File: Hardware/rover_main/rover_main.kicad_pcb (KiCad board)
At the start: 2 copper layers, 80 x 70 mm, 19 parts, among them J1 BATT, J2 BME280, J3 CSS811, J4 DRIVERS, J7 FTDI, J8 PROG, U1 LD1117A33, U2 MCP732831CHARGER, U3 ESP32-CAM

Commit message: change diode in pcb
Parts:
- moved D1 10.5 mm to (142.5, 92.5), turned to 0 degrees
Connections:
- C1 pad 1: Net-(C1-Pad1) -> VCC
- D1 pad 1: Net-(C1-Pad1) -> VCC
- D1 pad 2: VCC -> /BATT
- U1 pad 3: Net-(C1-Pad1) -> VCC
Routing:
- net VCC: track 49.2 -> 70.6 mm
- net Net-(C1-Pad1): track 14.9 -> 0.00 mm
- net /BATT: track 12.1 -> 24.7 mm

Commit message: Asig. places componets
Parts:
- added J10: Analog, Connector_PinHeader_2.54mm:PinHeader_1x12_P2.54mm_Vertical, F.Cu at (167.0, 97.2)
- added J5: GY-87, Connector_PinHeader_2.54mm:PinHeader_1x08_P2.54mm_Vertical, F.Cu at (146.2, 113.8)
- added J6: PROG, Connector_PinSocket_2.54mm:PinSocket_1x02_P2.54mm_Vertical, F.Cu at (131.9, 117.7)
- added J9: i2c, Connector_PinHeader_2.54mm:PinHeader_1x02_P2.54mm_Vertical, F.Cu at (163.6, 80.7)
- added JP1: Engine 2B, Jumper:SolderJumper-2_P1.3mm_Bridged_RoundedPad1.0x1.5mm, B.Cu at (124.4, 83.0)
- added JP10: Engine 2B, Jumper:SolderJumper-2_P1.3mm_Open_RoundedPad1.0x1.5mm, B.Cu at (144.4, 88.1)
- added JP11: SDE ESP, Jumper:SolderJumper-2_P1.3mm_Bridged_RoundedPad1.0x1.5mm, B.Cu at (120.0, 100.8)
- added JP12: SCL ESP, Jumper:SolderJumper-2_P1.3mm_Bridged_RoundedPad1.0x1.5mm, B.Cu at (120.2, 98.1)
- added JP2: Engine 1A, Jumper:SolderJumper-2_P1.3mm_Bridged_RoundedPad1.0x1.5mm, B.Cu at (131.9, 83.0)
- added JP3: Engine 2A, Jumper:SolderJumper-2_P1.3mm_Bridged_RoundedPad1.0x1.5mm, B.Cu at (126.9, 83.0)
- added JP4: Engine 1B, Jumper:SolderJumper-2_P1.3mm_Bridged_RoundedPad1.0x1.5mm, B.Cu at (129.4, 83.0)
- added JP5: SDA, Jumper:SolderJumper-2_P1.3mm_Open_RoundedPad1.0x1.5mm, B.Cu at (157.2, 80.7)
- added JP6: SCL, Jumper:SolderJumper-2_P1.3mm_Open_RoundedPad1.0x1.5mm, B.Cu at (157.2, 78.2)
- added JP7: Engine 1A, Jumper:SolderJumper-2_P1.3mm_Open_RoundedPad1.0x1.5mm, B.Cu at (144.4, 93.2)
- added JP8: Engine 1B, Jumper:SolderJumper-2_P1.3mm_Open_RoundedPad1.0x1.5mm, B.Cu at (144.4, 95.6)
- added JP9: Engine 2A, Jumper:SolderJumper-2_P1.3mm_Open_RoundedPad1.0x1.5mm, B.Cu at (144.4, 90.6)
- J8: value PROG -> Digital; footprint Connector_PinSocket_2.54mm:PinSocket_1x02_P2.54mm_Vertical -> Connector_PinHeader_2.54mm:PinHeader_1x12_P2.54mm_Vertical
- moved D2 76.2 mm to (175.7, 129.8), turned to 90 degrees
- moved J2 67.9 mm to (163.5, 123.1), turned to 270 degrees
- moved R1 66.6 mm to (182.2, 122.8), turned to 270 degrees
- moved J3 55.3 mm to (131.5, 123.0), turned to 90 degrees
- moved C3 53.8 mm to (181.9, 75.2), turned to 180 degrees
- moved U1 53.6 mm to (183.6, 116.6), turned to 90 degrees
- moved J8 50.9 mm to (151.8, 69.2), turned to 0 degrees
- moved J4 45.2 mm to (121.9, 77.9), turned to 90 degrees
- moved C2 44.6 mm to (175.4, 116.6), turned to 270 degrees
- moved REF** 40.2 mm to (196.5, 140.0)
- moved U2 35.6 mm to (179.7, 88.1), turned to 0 degrees
- moved REF** 34.9 mm to (196.5, 70.0)
- moved J1 34.5 mm to (191.9, 82.4), turned to 270 degrees
- moved D1 34.3 mm to (174.7, 104.5)
- moved C1 34.0 mm to (175.3, 109.9), turned to 270 degrees
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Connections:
- J8 pad 1: /GPIO0 -> /RX
- J8 pad 2: GND -> /TX
- U3 pad 11: /GPIO12 -> /GPIO12E
- U3 pad 12: /GPIO13 -> /GPIO13E
- U3 pad 13: /GPIO15 -> /GPIO15E
- U3 pad 14: /GPIO14 -> /GPIO14E
- U3 pad 15: /SDA -> /SDAE
- U3 pad 7: /SCL -> /SCLE
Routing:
- net +3V3: track 126.8 -> 10.6 mm
- net /SCLE: track 0.00 -> 78.1 mm
- net VCC: track 70.6 -> 0.00 mm
- net /SCL: track 70.3 -> 0.00 mm
- net /SDA: track 42.9 -> 0.00 mm
- net /GPIO12: track 51.2 -> 12.8 mm
- net /GPIO13: track 52.9 -> 17.2 mm
- net /GPIO14: track 59.9 -> 25.1 mm
- net /GPIO15: track 55.8 -> 21.3 mm
- net /BATT: track 24.7 -> 0.00 mm
- net /RX: track 14.6 -> 0.00 mm
- net /TX: track 14.6 -> 0.00 mm
- net GND: track 12.0 -> 0.00 mm
- net /GPIO14E: track 0.00 -> 5.29 mm
- net /GPIO12E: track 0.00 -> 5.29 mm
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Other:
- board size 80 x 70 mm -> 100 x 80 mm

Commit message: RE-ROUTEO
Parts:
- removed the REF** at (106.0, 140.0)
- removed the REF** at (106.5, 70.0)
- removed the REF** at (196.5, 70.0)
- removed the REF** at (196.5, 140.0)
- added REF**: MountingHole_3.2mm_M3_Pad_Via, MountingHole:MountingHole_3.2mm_M3_Pad_Via, F.Cu at (105.0, 125.0)
- added REF**: MountingHole_3.2mm_M3_Pad_Via, MountingHole:MountingHole_3.2mm_M3_Pad_Via, F.Cu at (105.0, 65.1)
- added REF**: MountingHole_3.2mm_M3_Pad_Via, MountingHole:MountingHole_3.2mm_M3_Pad_Via, F.Cu at (180.5, 65.0)
- added REF**: MountingHole_3.2mm_M3_Pad_Via, MountingHole:MountingHole_3.2mm_M3_Pad_Via, F.Cu at (180.0, 125.0)
- J2: footprint Connector_PinHeader_2.54mm:PinHeader_1x04_P2.54mm_Vertical -> Connector_PinHeader_2.54mm:PinHeader_1x06_P2.54mm_Vertical
- moved JP6 27.1 mm to (152.1, 104.8), turned to 270 degrees
- moved J2 25.7 mm to (139.4, 114.3)
- moved JP8 24.4 mm to (135.9, 72.8), turned to 90 degrees
- moved JP5 24.2 mm to (154.7, 104.8), turned to 270 degrees
- moved JP12 21.7 mm to (141.0, 104.5), turned to 270 degrees
- moved JP7 21.3 mm to (138.4, 72.8), turned to 90 degrees
- moved JP11 18.8 mm to (138.4, 104.5), turned to 270 degrees
- moved JP9 18.2 mm to (141.0, 72.8), turned to 90 degrees
- moved J1 16.6 mm to (179.0, 72.0)
- moved J3 15.8 mm to (144.8, 114.2)
- moved JP10 15.4 mm to (143.5, 72.8), turned to 90 degrees
- moved C3 12.1 mm to (170.0, 77.1), turned to 90 degrees
- moved U3 10.8 mm to (124.7, 89.8)
- moved D2 10.5 mm to (168.4, 122.3), turned to 0 degrees
- moved JP1 10.5 mm to (122.6, 72.8)
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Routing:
- net +3V3: track 10.6 -> 168.8 mm, vias 0 -> 1
- net VCC: track 0.00 -> 157.8 mm, vias 0 -> 2
- net /RX: track 0.00 -> 87.4 mm
- net /TX: track 0.00 -> 86.0 mm
- net /SDAB: track 0.00 -> 76.2 mm, vias 0 -> 1
- net /SCLB: track 0.00 -> 73.4 mm, vias 0 -> 1
- net /SCLE: track 78.1 -> 13.1 mm
- net /A1: track 0.00 -> 58.9 mm
- net /A3: track 0.00 -> 58.7 mm
- net /11: track 0.00 -> 52.3 mm
- net /SDAE: track 0.00 -> 49.7 mm
- net /SDA: track 0.00 -> 48.6 mm
- net /SCL: track 0.00 -> 40.8 mm
- net /BATT: track 0.00 -> 26.7 mm
- net /9: track 0.00 -> 24.0 mm
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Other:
- board size 100 x 80 mm -> 85 x 70 mm

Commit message: Update traces
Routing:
- net +3V3: track 168.8 -> 182.7 mm
- net /SCL: track 40.8 -> 52.4 mm
- net /TX: track 86.0 -> 77.5 mm
- net /RX: track 87.4 -> 79.6 mm
- net /SDA: track 48.6 -> 51.7 mm
- net /A3: track 58.7 -> 61.6 mm
- net /11: track 52.3 -> 55.2 mm
- net /A1: track 58.9 -> 61.4 mm
- net /SDAB: track 76.2 -> 77.2 mm
- net /BATT: track 26.7 -> 26.2 mm
- net VCC: track 157.8 -> 157.9 mm, vias 2 -> 0
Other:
- net class Default: clearance 0.2 -> 0.3
- rule trace_clearance: 0.2 -> 0.3

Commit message: Labels
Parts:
- moved JP5 0.22 mm to (154.7, 104.5)
- moved JP6 0.22 mm to (152.1, 104.5)
- renumbered J9 to I2C
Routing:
- net /SCLE: track 13.1 -> 10.4 mm
- net /SDAB: track 77.2 -> 78.0 mm
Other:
- outline, holes or cut-outs redrawn
- board text added: "3V3"
- board text added: "A"
- board text added: "B"
- board text added: "BAST PRO-MINI"
- board text added: "CHARGER"
- board text added: "CTS"
- board text added: "DRIVERS BATS"
- board text added: "DRIVERS ESP"
- board text added: "DTR"
- board text added: "ENGINES"
- board text added: "Engine 1"
- board text added: "Engine 2"
- board text added: "GND"
- board text added: "I2C BATS"
- board text added: "I2C ESP"
- board text added: "RX"
- board text added: "TX"
- board text added: "VCC"

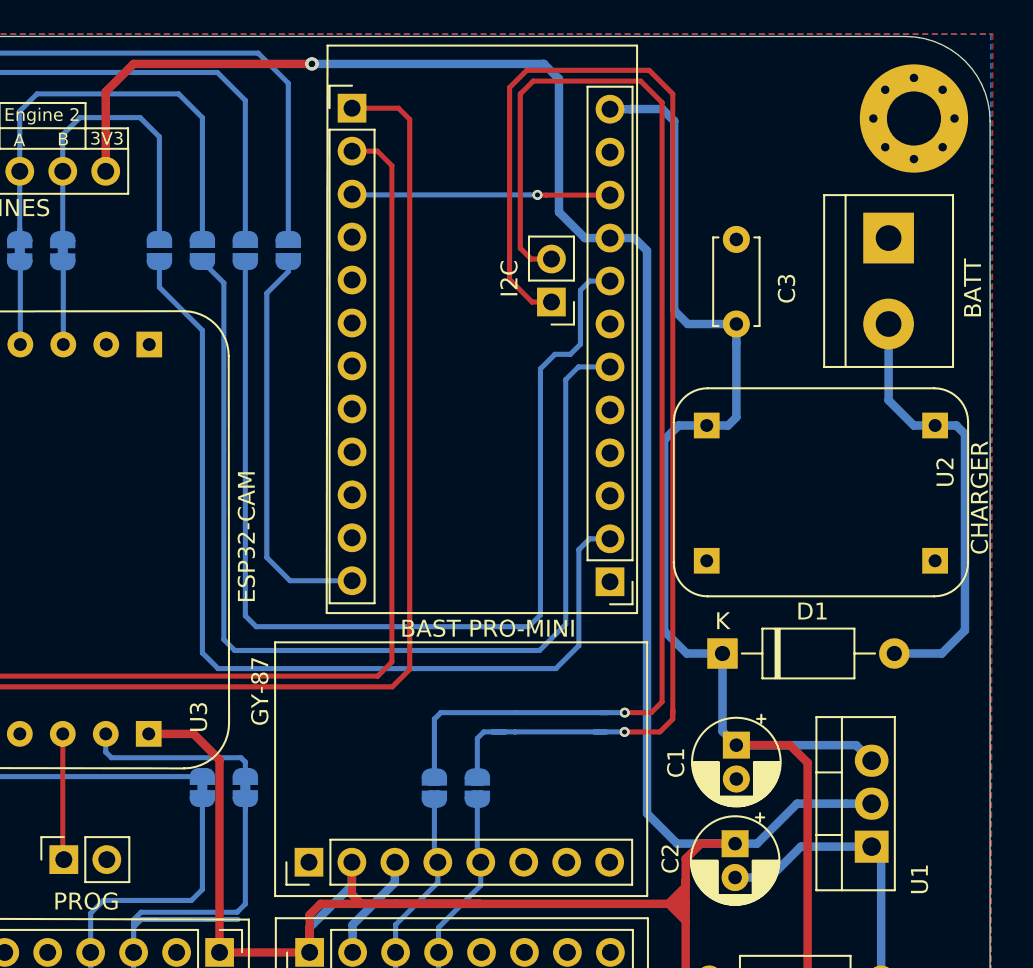
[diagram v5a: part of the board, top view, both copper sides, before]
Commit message: ADD DIODE
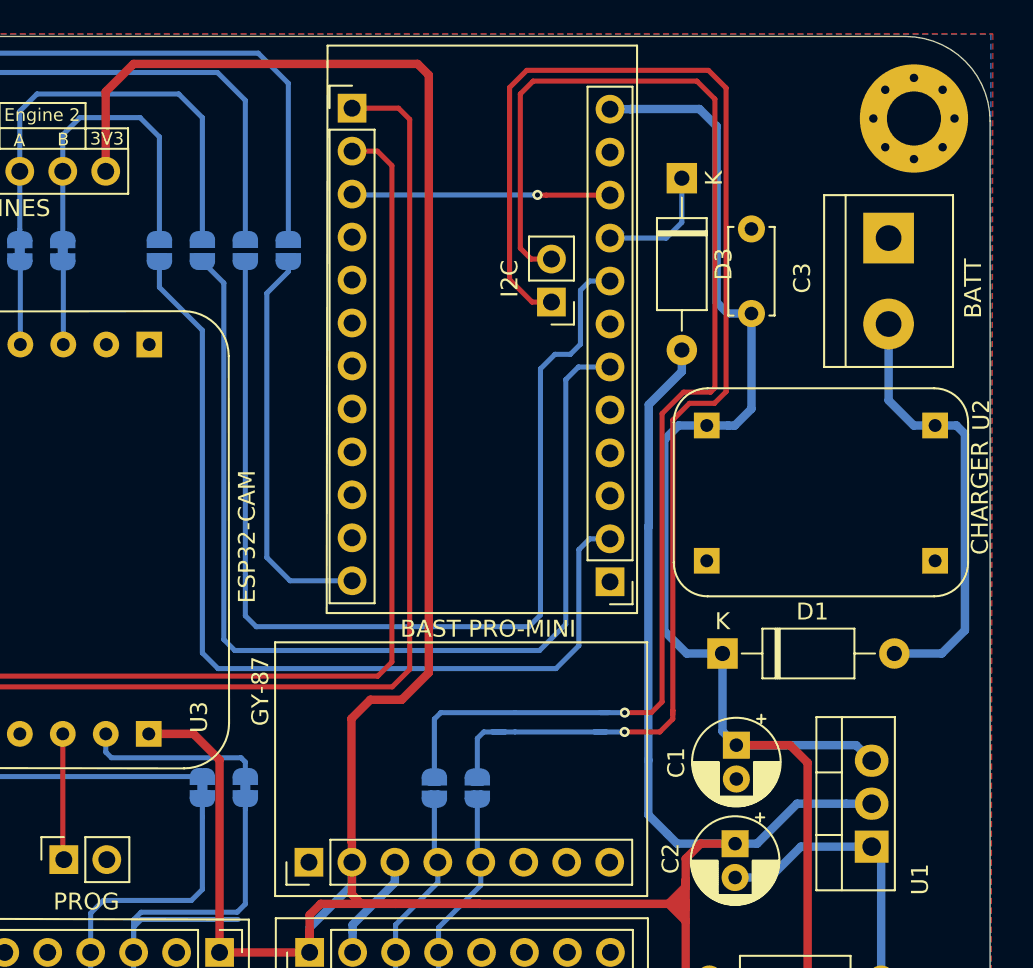
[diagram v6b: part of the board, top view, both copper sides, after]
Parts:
- added D3: D_Schottky, Diode_THT:D_A-405_P10.16mm_Horizontal, F.Cu at (166.8, 68.5)
- moved C3 1.09 mm to (170.9, 76.5)
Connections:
- J10 pad 9: +3V3 -> Net-(D3-Pad1)
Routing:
- net +3V3: track 182.7 -> 205.3 mm, vias 1 -> 0
- net Net-(D3-Pad1): track 0.00 -> 7.54 mm
- net /SDAB: track 78.0 -> 83.5 mm
- net /SCLB: track 73.7 -> 79.1 mm
- net VCC: track 157.9 -> 159.3 mm

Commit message: move  V track
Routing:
- net +3V3: track 205.3 -> 206.2 mm
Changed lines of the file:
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@@
     (thickness 1.6)
     (drawings 6343)
-    (tracks 305)
+    (tracks 308)
     (zones 0)
     (modules 36)
@@
   (segment (start 167.005 109.982) (end 167.005 111.252) (width 0.5) (layer F.Cu) (net 2))
   (segment (start 166.751 111.252) (end 166.497 111.506) (width 0.5) (layer F.Cu) (net 2))
-  (segment (start 147.27 108.92) (end 147.27 110.821) (width 0.5) (layer F.Cu) (net 2))
-  (segment (start 147.828 111.379) (end 149.86 111.379) (width 0.5) (layer F.Cu) (net 2))
-  (segment (start 147.27 110.821) (end 147.828 111.379) (width 0.5) (layer F.Cu) (net 2))
   (segment (start 144.769 114.254) (end 144.773 114.25) (width 0.5) (layer F.Cu) (net 2))
   (segment (start 139.445 114.254) (end 144.769 114.254) (width 0.5) (layer F.Cu) (net 2))
   (segment (start 144.773 114.25) (end 144.773 112.9) (width 0.5) (layer F.Cu) (net 2))
-  (segment (start 154.827 111.379) (end 145.431 111.379) (width 0.5) (layer F.Cu) (net 2))
   (segment (start 149.86 111.379) (end 154.827 111.379) (width 0.5) (layer F.Cu) (net 2))
   (segment (start 154.827 111.379) (end 165.989 111.379) (width 0.5) (layer F.Cu) (net 2))
@@
   (segment (start 164.7952 102.8954) (end 164.7952 106.1212) (width 0.5) (layer B.Cu) (net 2))
   (segment (start 164.7952 89.0778) (end 164.7952 102.8954) (width 0.5) (layer B.Cu) (net 2))
-  (segment (start 132.715 68.072) (end 132.715 63.373) (width 0.5) (layer F.Cu) (net 2))
-  (segment (start 132.715 63.373) (end 134.366 61.722) (width 0.5) (layer F.Cu) (net 2))
-  (segment (start 151.8158 97.7138) (end 151.8158 62.3824) (width 0.5) (layer F.Cu) (net 2))
-  (segment (start 150.2156 99.314) (end 151.8158 97.7138) (width 0.5) (layer F.Cu) (net 2))
-  (segment (start 134.366 61.722) (end 151.1554 61.722) (width 0.5) (layer F.Cu) (net 2))
-  (segment (start 147.27 108.92) (end 147.27 107.717919) (width 0.5) (layer F.Cu) (net 2))
-  (segment (start 148.3614 99.314) (end 150.2156 99.314) (width 0.5) (layer F.Cu) (net 2))
-  (segment (start 147.27 107.717919) (end 147.2438 107.691719) (width 0.5) (layer F.Cu) (net 2))
+  (segment (start 147.27 108.92) (end 147.27 106.5776) (width 0.5) (layer F.Cu) (net 2))
+  (segment (start 132.715 63.373) (end 132.715 68.072) (width 0.5) (layer F.Cu) (net 2))
+  (segment (start 147.27 106.5776) (end 151.8158 102.0318) (width 0.5) (layer F.Cu) (net 2))
+  (segment (start 151.8158 102.0318) (end 151.8158 62.3824) (width 0.5) (layer F.Cu) (net 2))
   (segment (start 151.8158 62.3824) (end 151.1554 61.722) (width 0.5) (layer F.Cu) (net 2))
-  (segment (start 147.2438 107.691719) (end 147.2438 100.4316) (width 0.5) (layer F.Cu) (net 2))
-  (segment (start 147.2438 100.4316) (end 148.3614 99.314) (width 0.5) (layer F.Cu) (net 2))
+  (segment (start 151.1554 61.722) (end 134.366 61.722) (width 0.5) (layer F.Cu) (net 2))
+  (segment (start 134.366 61.722) (end 132.715 63.373) (width 0.5) (layer F.Cu) (net 2))
+  (segment (start 147.1922 110.821) (end 146.6342 111.379) (width 0.5) (layer F.Cu) (net 2))
+  (segment (start 147.27 110.821) (end 147.1922 110.821) (width 0.5) (layer F.Cu) (net 2))
+  (segment (start 154.827 111.379) (end 146.6342 111.379) (width 0.5) (layer F.Cu) (net 2))
+  (segment (start 146.6342 111.379) (end 145.431 111.379) (width 0.5) (layer F.Cu) (net 2))
+  (segment (start 147.27 110.821) (end 147.828 111.379) (width 0.5) (layer F.Cu) (net 2))
+  (segment (start 147.27 110.6686) (end 147.9804 111.379) (width 0.5) (layer F.Cu) (net 2))
+  (segment (start 147.27 110.5146) (end 147.27 110.6686) (width 0.5) (layer F.Cu) (net 2))
+  (segment (start 147.9804 111.379) (end 149.86 111.379) (width 0.5) (layer F.Cu) (net 2))
+  (segment (start 147.828 111.379) (end 147.9804 111.379) (width 0.5) (layer F.Cu) (net 2))
+  (segment (start 147.27 110.5146) (end 147.27 110.821) (width 0.5) (layer F.Cu) (net 2))
+  (segment (start 147.27 108.92) (end 147.27 110.5146) (width 0.5) (layer F.Cu) (net 2))
   (segment (start 177.08 102) (end 178 102.92) (width 0.5) (layer B.Cu) (net 3))
   (segment (start 170 102) (end 177.08 102) (width 0.5) (layer B.Cu) (net 3))
